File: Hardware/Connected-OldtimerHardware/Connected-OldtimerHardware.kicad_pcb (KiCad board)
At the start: 2 copper layers, 1 part, among them U1 electron

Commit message: layout v1
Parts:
- added C1: 1uF, Capacitor_THT:C_Disc_D4.7mm_W2.5mm_P5.00mm, F.Cu at (185.2, 95.0)
- added D1: DIODE, Diode_THT:D_A-405_P10.16mm_Horizontal, F.Cu at (185.9, 81.2)
- added D2: D_Zener, Diode_THT:D_A-405_P7.62mm_Horizontal, F.Cu at (175.3, 95.2)
- added F1: Polyfuse 2000mA, Fuse:Fuse_Littelfuse-LVR200, F.Cu at (164.3, 107.3)
- added F2: Polyfuse 1000mA, Fuse:Fuse_Littelfuse-LVR200, F.Cu at (164.3, 114.8)
- added F3: Polyfuse SMD 1000mA, Capacitor_SMD:C_1210_3225Metric_Pad1.42x2.65mm_HandSolder, F.Cu at (169.6, 114.8)
- added F4: Polyfuse SMD 2000mA, Capacitor_SMD:C_1210_3225Metric_Pad1.42x2.65mm_HandSolder, F.Cu at (170.0, 107.3)
- added J1: CAN_Bus_Connector, Connector_JST:JST_XH_B04B-XH-A_1x04_P2.50mm_Vertical, F.Cu at (197.8, 79.5)
- added J2: MainConnector, Connector_JST:JST_XH_B03B-XH-A_1x03_P2.50mm_Vertical, F.Cu at (197.7, 111.5)
- added J3: NextionConnector, Connector_JST:JST_XH_B05B-XH-A_1x05_P2.50mm_Vertical, F.Cu at (197.8, 97.9)
- added J4: Conn_01x04, Connector_JST:JST_XH_B04B-XH-A_1x04_P2.50mm_Vertical, F.Cu at (108.2, 114.3)
- added Q1: 2N3906, Package_TO_SOT_THT:TO-92_Inline, F.Cu at (181.5, 72.3)
- added R1: 7.5K, Resistor_THT:R_Axial_DIN0207_L6.3mm_D2.5mm_P10.16mm_Horizontal, F.Cu at (189.5, 91.4)
- added R2: 10K, Resistor_THT:R_Axial_DIN0207_L6.3mm_D2.5mm_P10.16mm_Horizontal, F.Cu at (175.2, 90.9)
- added R3: 47K, Resistor_THT:R_Axial_DIN0207_L6.3mm_D2.5mm_P10.16mm_Horizontal, F.Cu at (185.6, 77.3)
- added R4: 10K, Resistor_THT:R_Axial_DIN0207_L6.3mm_D2.5mm_P10.16mm_Horizontal, F.Cu at (185.4, 67.8)
- added R5: 31K, Resistor_THT:R_Axial_DIN0207_L6.3mm_D2.5mm_P10.16mm_Horizontal, F.Cu at (181.8, 102.8)
- added R6: 4.7K, Resistor_THT:R_Axial_DIN0207_L6.3mm_D2.5mm_P10.16mm_Horizontal, F.Cu at (178.6, 92.7)
- added REF**: NextionMountingHoles, heathsfootprints:NextionMountingHoles, F.Cu at (96.4, 67.0)
- added U2: TSR_2-2450, heathsfootprints:heathsTRS_2_2450, F.Cu at (187.5, 102.6)
- added U3: CANTranceiverModule, heathsfootprints:CAN_Tranceiver_Module, F.Cu at (154.6, 79.3)
- added U4: AdafruitFRAM, heathsfootprints:Adafruit_I2C_FRAM, F.Cu at (131.0, 76.2)
- added U5: AdafruitUltimateGPS, heathsfootprints:AdafruitUltimateGPS, F.Cu at (108.7, 94.5)
- added U6: MotionSensor, heathsfootprints:ShockSensor, F.Cu at (130.7, 110.3)
- added U7: SFH618A-2, Package_DIP:DIP-4_W7.62mm_Socket, F.Cu at (179.2, 89.4)
- U1: value electron -> ParticleElectron
- moved U1 126.3 mm to (172.9, 92.5), turned to 90 degrees
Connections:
- U1 pad 1: (no net) -> 5VDC
- U1 pad 10: (no net) -> Net-(U1-Pad10)
- U1 pad 11: (no net) -> Net-(U1-Pad11)
- U1 pad 12: (no net) -> Net-(U1-Pad12)
- U1 pad 13: (no net) -> Net-(U1-Pad13)
- U1 pad 14: (no net) -> VMON
- U1 pad 15: (no net) -> AUX_1
- U1 pad 16: (no net) -> AUX_2
- U1 pad 17: (no net) -> Net-(U1-Pad17)
- U1 pad 18: (no net) -> Net-(U1-Pad18)
- U1 pad 19: (no net) -> GPS_TX
- U1 pad 2: (no net) -> GND
- U1 pad 20: (no net) -> GPS_RX
- U1 pad 21: (no net) -> Nextion_TX
- U1 pad 22: (no net) -> Nextion_RX
- U1 pad 23: (no net) -> CAN_TX
- U1 pad 24: (no net) -> CAN_RX
- U1 pad 25: (no net) -> FRAM_SDA
- U1 pad 26: (no net) -> FRAM_SCL
- U1 pad 27: (no net) -> Net-(U1-Pad27)
- U1 pad 28: (no net) -> Net-(U1-Pad28)
- U1 pad 29: (no net) -> Net-(U1-Pad29)
- U1 pad 3: (no net) -> TX
- U1 pad 30: (no net) -> Net-(U1-Pad30)
- U1 pad 31: (no net) -> Net-(U1-Pad31)
- U1 pad 32: (no net) -> Net-(U1-Pad32)
- U1 pad 33: (no net) -> GND
- U1 pad 34: (no net) -> VBAT
- U1 pad 35: (no net) -> RESET
- U1 pad 36: (no net) -> 3V3
- U1 pad 4: (no net) -> RX
- U1 pad 5: (no net) -> Shock_Signal
- U1 pad 6: (no net) -> DAC
- U1 pad 7: (no net) -> Net-(U1-Pad7)
- U1 pad 8: (no net) -> Net-(U1-Pad8)
- U1 pad 9: (no net) -> AUX_3
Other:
- board text added: "AUX"
- board text added: "CAN"
- board text added: "Display"
- board text added: "IGN"

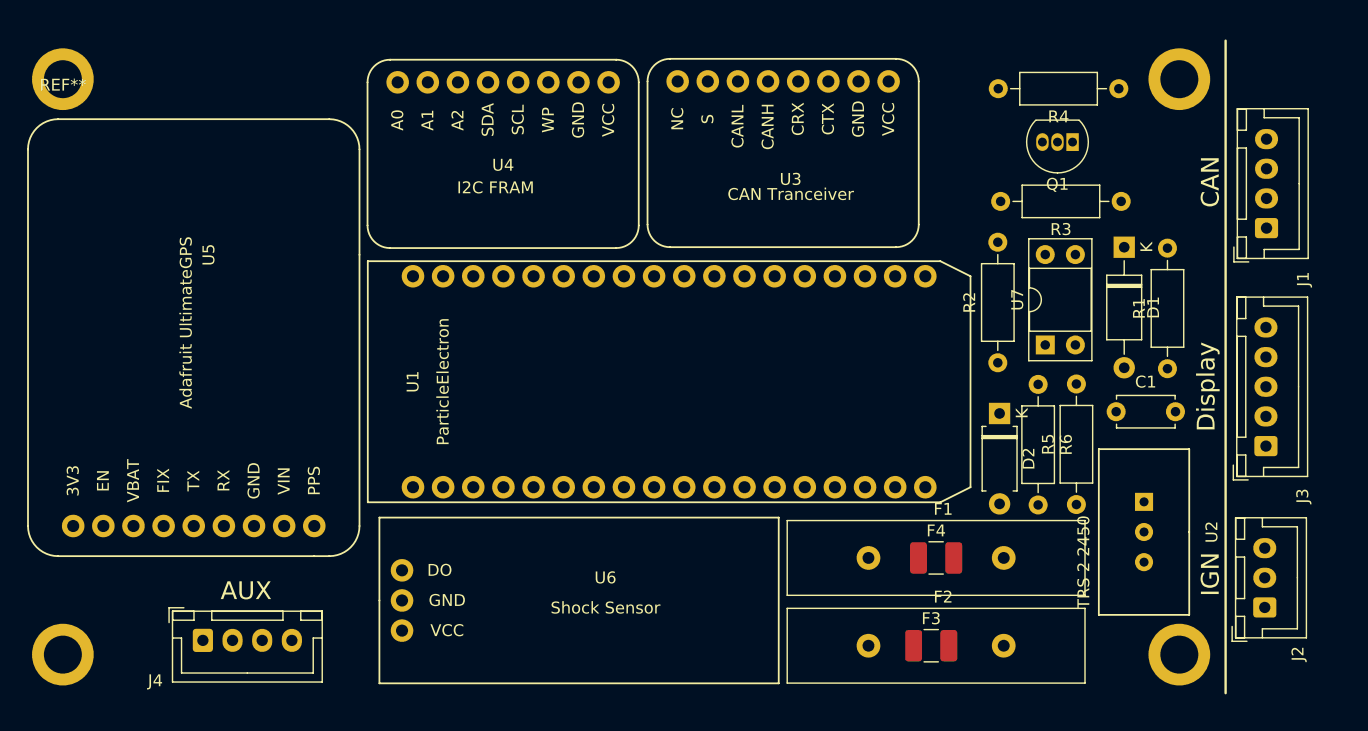
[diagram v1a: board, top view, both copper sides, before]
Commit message: all connections except ground and 5v
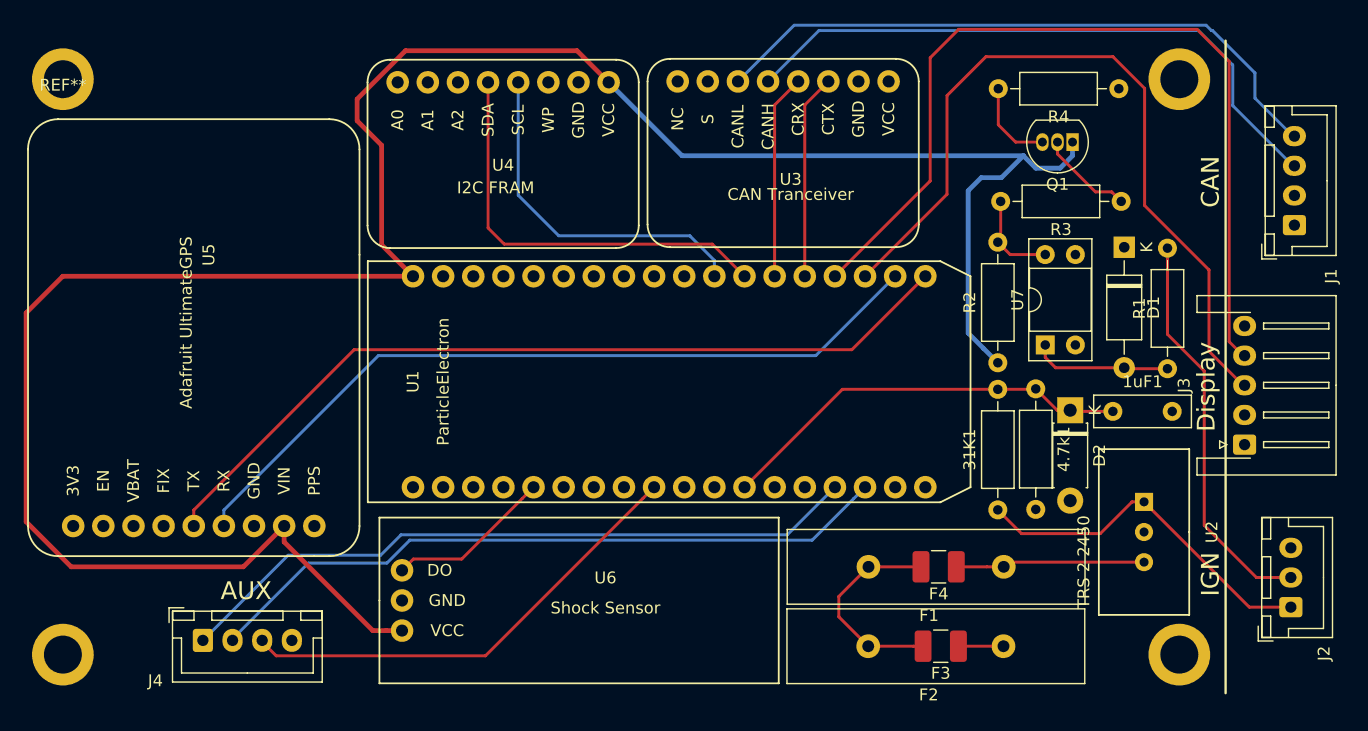
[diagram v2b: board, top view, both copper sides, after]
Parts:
- removed C1: 1uF, Capacitor_THT:C_Disc_D4.7mm_W2.5mm_P5.00mm
- removed R5: 31K, Resistor_THT:R_Axial_DIN0207_L6.3mm_D2.5mm_P10.16mm_Horizontal
- removed R6: 4.7K, Resistor_THT:R_Axial_DIN0207_L6.3mm_D2.5mm_P10.16mm_Horizontal
- added 1uF1: C, Capacitor_THT:C_Disc_D8.0mm_W2.5mm_P5.00mm, F.Cu at (184.9, 95.0)
- added 31K1: R_US, Resistor_THT:R_Axial_DIN0207_L6.3mm_D2.5mm_P10.16mm_Horizontal, F.Cu at (175.2, 103.3)
- added 4.7k1: R_US, Resistor_THT:R_Axial_DIN0207_L6.3mm_D2.5mm_P10.16mm_Horizontal, F.Cu at (178.4, 93.1)
- D2: footprint Diode_THT:D_A-405_P7.62mm_Horizontal -> Diode_THT:D_DO-41_SOD81_P7.62mm_Horizontal
- J3: footprint Connector_JST:JST_XH_B05B-XH-A_1x05_P2.50mm_Vertical -> Connector_JST:JST_XH_S05B-XH-A-1_1x05_P2.50mm_Horizontal
- J4: value Conn_01x04 -> AUXConnector
- moved F1 11.4 mm to (175.7, 108.1), turned to 180 degrees
- moved F2 11.4 mm to (175.7, 114.8), turned to 180 degrees
- moved D2 5.96 mm to (181.3, 94.9)
- moved J1 2.36 mm to (200.2, 79.3)
- moved J2 2.20 mm to (199.9, 111.5)
- moved J3 1.80 mm to (196.0, 97.8)
- moved F3 0.80 mm to (170.4, 114.8), turned to 180 degrees
- moved F4 0.78 mm to (170.2, 108.1), turned to 180 degrees
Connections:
- U1 pad 12: Net-(U1-Pad12) -> VMON
- U1 pad 14: VMON -> Net-(U1-Pad14)
- U4 pad 8: 5VDC -> 3V3
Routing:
- net 3V3: track 0.00 -> 196.6 mm
- net Nextion_RX: track 0.00 -> 74.5 mm
- net GPS_TX: track 0.00 -> 71.2 mm
- net GPS_RX: track 0.00 -> 66.1 mm
- net Nextion_TX: track 0.00 -> 65.8 mm
- net AUX_2: track 0.00 -> 58.7 mm
- net AUX_1: track 0.00 -> 58.6 mm
- net CAN_L: track 0.00 -> 54.0 mm
- net CAN_H: track 0.00 -> 52.9 mm
- net AUX_3: track 0.00 -> 39.5 mm
- net FRAM_SDA: track 0.00 -> 35.6 mm
- net VMON: track 0.00 -> 35.3 mm
- net IGN: track 0.00 -> 33.8 mm
- net 12VIN: track 0.00 -> 30.3 mm
- net FRAM_SCL: track 0.00 -> 29.7 mm
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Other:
- net class thickbaby added: clearance 0.2, trace_width 0.4, via_dia 0.8, via_drill 0.4
- net class thicko added: clearance 0.2, trace_width 0.25, via_dia 0.8, via_drill 0.4

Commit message: fix
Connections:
- U1 pad 27: Net-(U1-Pad27) -> IGNSignal
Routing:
- net IGNSignal: track 7.36 -> 96.7 mm
- net Net-(F2-Pad1): track 3.80 -> 54.5 mm
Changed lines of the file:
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@@
     (thickness 1.6)
     (drawings 5)
-    (tracks 151)
+    (tracks 166)
     (zones 0)
     (modules 26)
-    (nets 58)
+    (nets 57)
   )
   (page A4)
@@
   (net 41 AUX_2)
   (net 42 AUX_3)
-  (net 43 "Net-(U1-Pad27)")
-  (net 44 "Net-(U1-Pad28)")
-  (net 45 "Net-(U1-Pad29)")
-  (net 46 "Net-(U1-Pad30)")
-  (net 47 "Net-(U1-Pad31)")
-  (net 48 "Net-(U1-Pad32)")
-  (net 49 "Net-(U1-Pad18)")
-  (net 50 "Net-(U1-Pad17)")
-  (net 51 "Net-(U1-Pad13)")
-  (net 52 "Net-(U1-Pad11)")
-  (net 53 "Net-(U1-Pad10)")
-  (net 54 "Net-(U1-Pad8)")
-  (net 55 "Net-(U1-Pad7)")
-  (net 56 VMON)
-  (net 57 "Net-(U1-Pad14)")
+  (net 43 "Net-(U1-Pad28)")
+  (net 44 "Net-(U1-Pad29)")
+  (net 45 "Net-(U1-Pad30)")
+  (net 46 "Net-(U1-Pad31)")
+  (net 47 "Net-(U1-Pad32)")
+  (net 48 "Net-(U1-Pad18)")
+  (net 49 "Net-(U1-Pad17)")
+  (net 50 "Net-(U1-Pad13)")
+  (net 51 "Net-(U1-Pad11)")
+  (net 52 "Net-(U1-Pad10)")
+  (net 53 "Net-(U1-Pad8)")
+  (net 54 "Net-(U1-Pad7)")
+  (net 55 VMON)
+  (net 56 "Net-(U1-Pad14)")
   (net_class Default "This is the default net class."
     (clearance 0.2)
@@
     (add_net "Net-(U1-Pad17)")
     (add_net "Net-(U1-Pad18)")
-    (add_net "Net-(U1-Pad27)")
     (add_net "Net-(U1-Pad28)")
     (add_net "Net-(U1-Pad29)")
@@
       (net 22 FRAM_SCL))
     (pad 27 thru_hole circle (at 8.89 -24.13 90) (size 1.9 1.9) (drill 1.02) (layers *.Cu *.Mask F.SilkS)
-      (net 43 "Net-(U1-Pad27)"))
+      (net 14 IGNSignal))
     (pad 28 thru_hole circle (at 8.89 -26.67 90) (size 1.9 1.9) (drill 1.02) (layers *.Cu *.Mask F.SilkS)
-      (net 44 "Net-(U1-Pad28)"))
+      (net 43 "Net-(U1-Pad28)"))
     (pad 29 thru_hole circle (at 8.89 -29.21 90) (size 1.9 1.9) (drill 1.02) (layers *.Cu *.Mask F.SilkS)
-      (net 45 "Net-(U1-Pad29)"))
+      (net 44 "Net-(U1-Pad29)"))
     (pad 30 thru_hole circle (at 8.89 -31.75 90) (size 1.9 1.9) (drill 1.02) (layers *.Cu *.Mask F.SilkS)
-      (net 46 "Net-(U1-Pad30)"))
+      (net 45 "Net-(U1-Pad30)"))
     (pad 31 thru_hole circle (at 8.89 -34.29 90) (size 1.9 1.9) (drill 1.02) (layers *.Cu *.Mask F.SilkS)
-      (net 47 "Net-(U1-Pad31)"))
+      (net 46 "Net-(U1-Pad31)"))
     (pad 32 thru_hole circle (at 8.89 -36.83 90) (size 1.9 1.9) (drill 1.02) (layers *.Cu *.Mask F.SilkS)
-      (net 48 "Net-(U1-Pad32)"))
+      (net 47 "Net-(U1-Pad32)"))
     (pad 33 thru_hole circle (at 8.89 -39.37 90) (size 1.9 1.9) (drill 1.02) (layers *.Cu *.Mask F.SilkS)
       (net 1 GND))
@@
       (net 15 3V3))
     (pad 18 thru_hole circle (at -8.89 -3.81 90) (size 1.9 1.9) (drill 1.02) (layers *.Cu *.Mask F.SilkS)
-      (net 49 "Net-(U1-Pad18)"))
+      (net 48 "Net-(U1-Pad18)"))
     (pad 17 thru_hole circle (at -8.89 -6.35 90) (size 1.9 1.9) (drill 1.02) (layers *.Cu *.Mask F.SilkS)
-      (net 50 "Net-(U1-Pad17)"))
+      (net 49 "Net-(U1-Pad17)"))
     (pad 16 thru_hole circle (at -8.89 -8.89 90) (size 1.9 1.9) (drill 1.02) (layers *.Cu *.Mask F.SilkS)
       (net 41 AUX_2))
@@
       (net 40 AUX_1))
     (pad 14 thru_hole circle (at -8.89 -13.97 90) (size 1.9 1.9) (drill 1.02) (layers *.Cu *.Mask F.SilkS)
-      (net 57 "Net-(U1-Pad14)"))
+      (net 56 "Net-(U1-Pad14)"))
     (pad 13 thru_hole circle (at -8.89 -16.51 90) (size 1.9 1.9) (drill 1.02) (layers *.Cu *.Mask F.SilkS)
-      (net 51 "Net-(U1-Pad13)"))
+      (net 50 "Net-(U1-Pad13)"))
     (pad 12 thru_hole circle (at -8.89 -19.05 90) (size 1.9 1.9) (drill 1.02) (layers *.Cu *.Mask F.SilkS)
-      (net 56 VMON))
+      (net 55 VMON))
     (pad 11 thru_hole circle (at -8.89 -21.59 90) (size 1.9 1.9) (drill 1.02) (layers *.Cu *.Mask F.SilkS)
-      (net 52 "Net-(U1-Pad11)"))
+      (net 51 "Net-(U1-Pad11)"))
     (pad 10 thru_hole circle (at -8.89 -24.13 90) (size 1.9 1.9) (drill 1.02) (layers *.Cu *.Mask F.SilkS)
-      (net 53 "Net-(U1-Pad10)"))
+      (net 52 "Net-(U1-Pad10)"))
     (pad 9 thru_hole circle (at -8.89 -26.67 90) (size 1.9 1.9) (drill 1.02) (layers *.Cu *.Mask F.SilkS)
       (net 42 AUX_3))
     (pad 8 thru_hole circle (at -8.89 -29.21 90) (size 1.9 1.9) (drill 1.02) (layers *.Cu *.Mask F.SilkS)
-      (net 54 "Net-(U1-Pad8)"))
+      (net 53 "Net-(U1-Pad8)"))
     (pad 7 thru_hole circle (at -8.89 -31.75 90) (size 1.9 1.9) (drill 1.02) (layers *.Cu *.Mask F.SilkS)
-      (net 55 "Net-(U1-Pad7)"))
+      (net 54 "Net-(U1-Pad7)"))
     (pad 6 thru_hole circle (at -8.89 -34.29 90) (size 1.9 1.9) (drill 1.02) (layers *.Cu *.Mask F.SilkS)
       (net 26 DAC))
@@
     )
     (pad 1 thru_hole circle (at 0 0) (size 1.6 1.6) (drill 0.8) (layers *.Cu *.Mask)
-      (net 56 VMON))
+      (net 55 VMON))
     (pad 2 thru_hole circle (at 5 0) (size 1.6 1.6) (drill 0.8) (layers *.Cu *.Mask)
       (net 1 GND))
@@
     (fp_line (start 1.93 -1.25) (end 1.93 1.25) (layer F.Fab) (width 0.1))
     (pad 2 thru_hole oval (at 10.16 0 90) (size 1.6 1.6) (drill 0.8) (layers *.Cu *.Mask)
-      (net 56 VMON))
+      (net 55 VMON))
     (pad 1 thru_hole circle (at 0 0 90) (size 1.6 1.6) (drill 0.8) (layers *.Cu *.Mask)
       (net 8 12VIN))
@@
     )
     (pad 1 thru_hole circle (at 0 0 270) (size 1.6 1.6) (drill 0.8) (layers *.Cu *.Mask)
-      (net 56 VMON))
+      (net 55 VMON))
     (pad 2 thru_hole oval (at 10.16 0 270) (size 1.6 1.6) (drill 0.8) (layers *.Cu *.Mask)
       (net 1 GND))
@@
     )
     (pad 1 thru_hole rect (at 0 0 270) (size 2.2 2.2) (drill 1.1) (layers *.Cu *.Mask)
-      (net 56 VMON))
+      (net 55 VMON))
     (pad 2 thru_hole oval (at 7.62 0 270) (size 2.2 2.2) (drill 1.1) (layers *.Cu *.Mask)
       (net 1 GND))
@@
   (segment (start 175.7 108.1) (end 174.285787 108.1) (width 0.25) (layer F.Cu) (net 4))
   (segment (start 175.678589 114.791319) (end 171.878589 114.791319) (width 0.25) (layer F.Cu) (net 5))
+  (segment (start 182.047443 114.791319) (end 182.056124 114.8) (width 0.25) (layer B.Cu) (net 5))
+  (segment (start 175.678589 114.791319) (end 182.047443 114.791319) (width 0.25) (layer B.Cu) (net 5))
+  (segment (start 182.056124 114.8) (end 184.3 114.8) (width 0.25) (layer B.Cu) (net 5))
+  (segment (start 200.2 98.9) (end 200.2 79.3) (width 0.25) (layer B.Cu) (net 5))
+  (segment (start 184.3 114.8) (end 200.2 98.9) (width 0.25) (layer B.Cu) (net 5))
   (segment (start 160.12522 62.9) (end 155.837201 67.188019) (width 0.25) (layer B.Cu) (net 6))
   (segment (start 192.1 62.9) (end 160.12522 62.9) (width 0.25) (layer B.Cu) (net 6))
@@
   (segment (start 184.800001 76.500001) (end 183.430001 76.500001) (width 0.25) (layer F.Cu) (net 13))
   (segment (start 185.6 77.3) (end 184.800001 76.500001) (width 0.25) (layer F.Cu) (net 13))
-  (segment (start 175.24 67.8) (end 175.24 70.84) (width 0.25) (layer F.Cu) (net 14))
-  (segment (start 176.7 72.3) (end 178.96 72.3) (width 0.25) (layer F.Cu) (net 14))
-  (segment (start 175.24 70.84) (end 176.7 72.3) (width 0.25) (layer F.Cu) (net 14))
+  (segment (start 175.24 67.8) (end 175.24 69.94) (width 0.25) (layer B.Cu) (net 14))
+  (segment (start 177.6 72.3) (end 178.96 72.3) (width 0.25) (layer B.Cu) (net 14))
+  (segment (start 175.24 69.94) (end 177.6 72.3) (width 0.25) (layer B.Cu) (net 14))
+  (segment (start 137.06718 81.6) (end 146.76 81.6) (width 0.25) (layer B.Cu) (net 14))
+  (segment (start 122.5 67.03282) (end 137.06718 81.6) (width 0.25) (layer B.Cu) (net 14))
+  (segment (start 122.5 66.3) (end 122.5 67.03282) (width 0.25) (layer B.Cu) (net 14))
+  (segment (start 146.84 69.94) (end 145.9 69) (width 0.25) (layer B.Cu) (net 14))
+  (segment (start 175.24 69.94) (end 146.84 69.94) (width 0.25) (layer B.Cu) (net 14))
+  (segment (start 145.9 69) (end 145.9 68.2) (width 0.25) (layer B.Cu) (net 14))
+  (segment (start 142.4 64.7) (end 124.1 64.7) (width 0.25) (layer B.Cu) (net 14))
+  (segment (start 146.76 81.6) (end 148.77 83.61) (width 0.25) (layer B.Cu) (net 14))
+  (segment (start 145.9 68.2) (end 142.4 64.7) (width 0.25) (layer B.Cu) (net 14))
+  (segment (start 124.1 64.7) (end 122.5 66.3) (width 0.25) (layer B.Cu) (net 14))
   (segment (start 111.61 108.1) (end 115.05 104.66) (width 0.4) (layer F.Cu) (net 15))
   (segment (start 97.1 108.1) (end 111.61 108.1) (width 0.4) (layer F.Cu) (net 15))
@@
   (segment (start 113.2 114.425) (end 114.37501 115.60001) (width 0.25) (layer F.Cu) (net 42))
   (segment (start 113.2 114.3) (end 113.2 114.425) (width 0.25) (layer F.Cu) (net 42))
-  (segment (start 162.1 93.14) (end 153.85 101.39) (width 0.25) (layer F.Cu) (net 56))
-  (segment (start 175.2 93.14) (end 162.1 93.14) (width 0.25) (layer F.Cu) (net 56))
-  (segment (start 178.36 93.14) (end 178.4 93.1) (width 0.25) (layer F.Cu) (net 56))
-  (segment (start 175.2 93.14) (end 178.36 93.14) (width 0.25) (layer F.Cu) (net 56))
-  (segment (start 180.2 94.9) (end 181.3 94.9) (width 0.25) (layer F.Cu) (net 56))
-  (segment (start 178.4 93.1) (end 180.2 94.9) (width 0.25) (layer F.Cu) (net 56))
-  (segment (start 181.4 95) (end 181.3 94.9) (width 0.25) (layer F.Cu) (net 56))
-  (segment (start 184.9 95) (end 181.4 95) (width 0.25) (layer F.Cu) (net 56))
+  (segment (start 162.1 93.14) (end 153.85 101.39) (width 0.25) (layer F.Cu) (net 55))
+  (segment (start 175.2 93.14) (end 162.1 93.14) (width 0.25) (layer F.Cu) (net 55))
+  (segment (start 178.36 93.14) (end 178.4 93.1) (width 0.25) (layer F.Cu) (net 55))
+  (segment (start 175.2 93.14) (end 178.36 93.14) (width 0.25) (layer F.Cu) (net 55))
+  (segment (start 180.2 94.9) (end 181.3 94.9) (width 0.25) (layer F.Cu) (net 55))
+  (segment (start 178.4 93.1) (end 180.2 94.9) (width 0.25) (layer F.Cu) (net 55))
+  (segment (start 181.4 95) (end 181.3 94.9) (width 0.25) (layer F.Cu) (net 55))
+  (segment (start 184.9 95) (end 181.4 95) (width 0.25) (layer F.Cu) (net 55))
 )

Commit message: completed tracks
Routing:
- net 5VDC: track 17.8 -> 143.0 mm, vias 0 -> 1
- added copper zone on B.Cu, net GND
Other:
- net class superthink added: clearance 0.3, trace_width 1, via_dia 0.8, via_drill 0.4

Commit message: minor changes
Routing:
- net Nextion_RX: track 74.5 -> 67.3 mm
- net IGNSignal: track 96.7 -> 103.0 mm
- net Nextion_TX: track 65.8 -> 62.4 mm
- net CAN_L: track 54.0 -> 51.5 mm

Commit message: changed up connectors
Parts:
- J1: value CAN_Bus_Connector -> NextionConnector; footprint Connector_JST:JST_XH_B04B-XH-A_1x04_P2.50mm_Vertical -> Connector_JST:JST_XH_S04B-XH-A-1_1x04_P2.50mm_Horizontal
- J3: value NextionConnector -> CAN_Bus_Connector; footprint Connector_JST:JST_XH_S05B-XH-A-1_1x05_P2.50mm_Horizontal -> Connector_JST:JST_XH_B05B-XH-A_1x05_P2.50mm_Vertical
- moved J3 19.7 mm to (200.0, 78.5)
- moved J1 17.8 mm to (195.9, 96.6)
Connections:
- J1 pad 1: Net-(F2-Pad1) -> GND
- J1 pad 2: GND -> Nextion_RX
- J1 pad 3: CAN_H -> Nextion_TX
- J1 pad 4: CAN_L -> 5VDC
- J3 pad 1: 5VDC -> GND
- J3 pad 2: GND -> CAN_H
- J3 pad 3: Nextion_TX -> CAN_L
- J3 pad 4: Nextion_RX -> Net-(F2-Pad1)
- U1 pad 27: IGNSignal -> Net-(U1-Pad27)
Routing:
- net 5VDC: track 143.0 -> 157.8 mm
- net Net-(F2-Pad1): track 54.3 -> 64.6 mm
- net Nextion_RX: track 67.3 -> 71.0 mm
- net CAN_H: track 52.6 -> 50.2 mm
- net Nextion_TX: track 62.4 -> 60.9 mm
- net 3V3: track 196.6 -> 197.5 mm
- net CAN_L: track 51.5 -> 52.4 mm
